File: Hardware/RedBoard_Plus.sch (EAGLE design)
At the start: 84 parts, among them IC3 LM1117, J1 DNP, J2 ISP, J3 5.5x2.1mm Barrel, J4 QWIIC_RIGHT_ANGLE, J5 USB Female Type C Connector, Q1 20V/4.2A/52mΩ/1.4W, Q2 310mA/60V/1.6Ω, Q3 310mA/60V/1.6Ω, U1 CH340G, U3 3.3V, U4 ATMEGA328P_TQFP, Y1 16MHz, Y2 12MHz

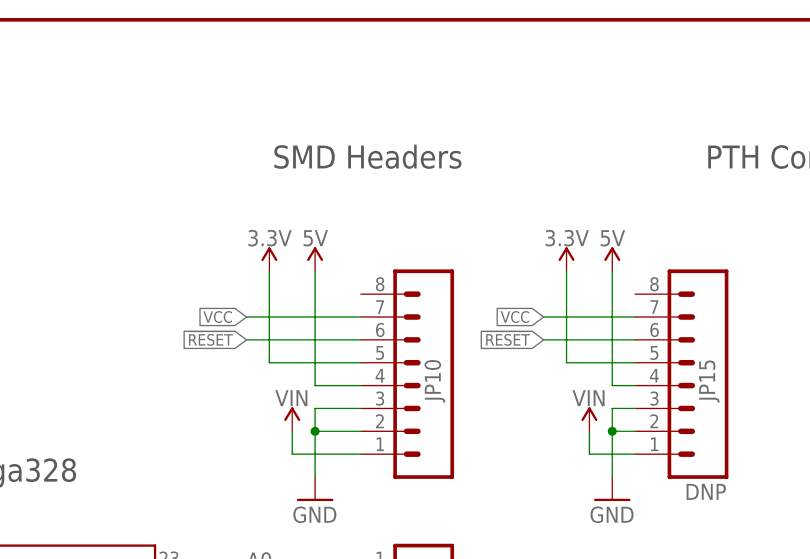
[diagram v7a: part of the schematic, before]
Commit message: Run engineering checklist
Changes made:
Flipped the V10 on the board edge
Changed the 2 VCC flags in the schematic to power symbols
Added the RedBoard logo to the SF Aesthetics library and replaced the device in the schematic
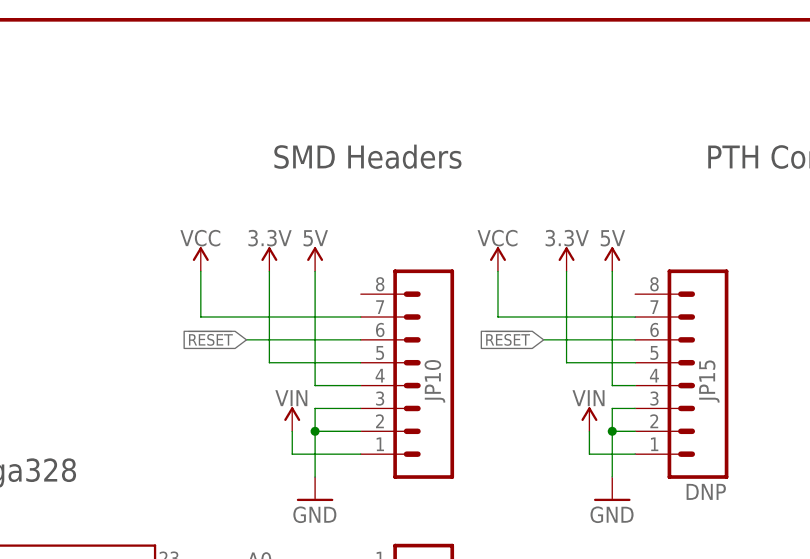
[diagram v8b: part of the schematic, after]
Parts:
- U$1, U$3: device redboard_logo:REDBOARD_LOGO -> SparkFun-Aesthetics:REDBOARD_LOGO
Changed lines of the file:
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@@
 <part name="FD1" library="SparkFun-Aesthetics" deviceset="FIDUCIAL" device="1X2"/>
 <part name="FD2" library="SparkFun-Aesthetics" deviceset="FIDUCIAL" device="1X2"/>
-<part name="U$1" library="redboard_logo" deviceset="REDBOARD_LOGO" device=""/>
-<part name="U$3" library="redboard_logo" deviceset="REDBOARD_LOGO" device=""/>
+<part name="U$1" library="SparkFun-Aesthetics" deviceset="REDBOARD_LOGO" device=""/>
+<part name="U$3" library="SparkFun-Aesthetics" deviceset="REDBOARD_LOGO" device=""/>
 <part name="SUPPLY25" library="SparkFun-PowerSymbols" deviceset="VIN" device=""/>
 <part name="U1" library="SparkFun-IC-Comms" deviceset="CH340G" device="SMD" value="CH340G"/>
@@
 <part name="GND19" library="SparkFun-PowerSymbols" deviceset="GND" device=""/>
 <part name="LOGO1" library="SparkFun-Aesthetics" deviceset="QWIIC_LOGO" device="_5MM" value="QWIIC_LOGO_5MM"/>
+<part name="SUPPLY7" library="SparkFun-PowerSymbols" deviceset="VCC" device=""/>
+<part name="SUPPLY26" library="SparkFun-PowerSymbols" deviceset="VCC" device=""/>
 </parts>
 <sheets>
@@
 </instance>
 <instance part="LOGO1" gate="G$1" x="218.44" y="7.62" smashed="yes"/>
+<instance part="SUPPLY7" gate="G$1" x="114.3" y="251.46" smashed="yes">
+<attribute name="VALUE" x="114.3" y="254.254" size="1.778" layer="96" font="vector" align="bottom-center"/>
+</instance>
+<instance part="SUPPLY26" gate="G$1" x="147.32" y="251.46" smashed="yes">
+<attribute name="VALUE" x="147.32" y="254.254" size="1.778" layer="96" font="vector" align="bottom-center"/>
+</instance>
 </instances>
 <busses>
@@
 </segment>
 <segment>
-<pinref part="JP10" gate="G$1" pin="7"/>
-<wire x1="132.08" y1="246.38" x2="119.38" y2="246.38" width="0.1524" layer="91"/>
-<label x="119.38" y="246.38" size="1.27" layer="95" font="vector" rot="R180" xref="yes"/>
-</segment>
-<segment>
 <pinref part="S2" gate="G$1" pin="2"/>
 <wire x1="241.3" y1="177.8" x2="238.76" y2="177.8" width="0.1524" layer="91"/>
@@
 </segment>
 <segment>
+<pinref part="JP10" gate="G$1" pin="7"/>
+<wire x1="132.08" y1="246.38" x2="114.3" y2="246.38" width="0.1524" layer="91"/>
+<wire x1="114.3" y1="246.38" x2="114.3" y2="251.46" width="0.1524" layer="91"/>
+<pinref part="SUPPLY7" gate="G$1" pin="VCC"/>
+</segment>
+<segment>
 <pinref part="JP15" gate="G$1" pin="7"/>
-<wire x1="162.56" y1="246.38" x2="152.4" y2="246.38" width="0.1524" layer="91"/>
-<label x="152.4" y="246.38" size="1.27" layer="95" font="vector" rot="R180" xref="yes"/>
-</segment>
-</net>
+<wire x1="162.56" y1="246.38" x2="147.32" y2="246.38" width="0.1524" layer="91"/>
+<wire x1="147.32" y1="246.38" x2="147.32" y2="251.46" width="0.1524" layer="91"/>
+<pinref part="SUPPLY26" gate="G$1" pin="VCC"/>
+</segment>
+</net>
